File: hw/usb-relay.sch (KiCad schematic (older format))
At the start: 22 parts, among them IC1 ATTINY85-P, K1 RELAY_2RT, P1 USB_B, P2 CONN_02X03, Q1 BC548, U1 LM741

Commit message: Changes
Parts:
- removed U1: LM741, Housings_DIP:DIP-8_W7.62mm, symbol LM741
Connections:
- wire segments 67 -> 56
- no-connect marks 6 -> 4
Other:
- moved on the sheet: R2, R3
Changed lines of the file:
@@
 L R R3
 U 1 1 56BF31DE
-P 4950 6100
-F 0 "R3" V 5030 6100 50  0000 C CNN
-F 1 "R" V 4950 6100 50  0000 C CNN
-F 2 "Resistors_ThroughHole:Resistor_Horizontal_RM10mm" V 4880 6100 50  0001 C CNN
-F 3 "" H 4950 6100 50  0000 C CNN
-	1    4950 6100
+P 3850 6000
+F 0 "R3" V 3930 6000 50  0000 C CNN
+F 1 "R" V 3850 6000 50  0000 C CNN
+F 2 "Resistors_ThroughHole:Resistor_Horizontal_RM10mm" V 3780 6000 50  0001 C CNN
+F 3 "" H 3850 6000 50  0000 C CNN
+	1    3850 6000
 	0    1    1    0
 $EndComp
@@
 L R R2
 U 1 1 56BF32F5
-P 4750 6250
-F 0 "R2" V 4830 6250 50  0000 C CNN
-F 1 "R" V 4750 6250 50  0000 C CNN
-F 2 "Resistors_ThroughHole:Resistor_Horizontal_RM10mm" V 4680 6250 50  0001 C CNN
-F 3 "" H 4750 6250 50  0000 C CNN
-	1    4750 6250
+P 3550 6100
+F 0 "R2" V 3630 6100 50  0000 C CNN
+F 1 "R" V 3550 6100 50  0000 C CNN
+F 2 "Resistors_ThroughHole:Resistor_Horizontal_RM10mm" V 3480 6100 50  0001 C CNN
+F 3 "" H 3550 6100 50  0000 C CNN
+	1    3550 6100
 	1    0    0    -1
 $EndComp
@@
 $EndComp
 $Comp
-L LM741 U1
-U 1 1 56BF4D2D
-P 5050 5450
-F 0 "U1" H 5050 5700 50  0000 L CNN
-F 1 "LM741" H 5050 5600 50  0000 L CNN
-F 2 "Housings_DIP:DIP-8_W7.62mm" H 5100 5500 50  0001 C CNN
-F 3 "" H 5200 5600 50  0000 C CNN
-	1    5050 5450
-	1    0    0    -1
-$EndComp
-$Comp
 L +5V #PWR03
 U 1 1 56BF5036
@@
 Wire Wire Line
 	3050 5300 3050 3900
-Wire Wire Line
-	3050 5300 4600 5300
-Wire Wire Line
-	4600 5300 4600 5350
-Wire Wire Line
-	4600 5350 4750 5350
-$Comp
-L +5V #PWR09
-U 1 1 56BF672A
-P 4950 5100
-F 0 "#PWR09" H 4950 4950 50  0001 C CNN
-F 1 "+5V" H 4950 5240 50  0000 C CNN
-F 2 "" H 4950 5100 50  0000 C CNN
-F 3 "" H 4950 5100 50  0000 C CNN
-	1    4950 5100
-	1    0    0    -1
-$EndComp
-$Comp
-L GND #PWR010
-U 1 1 56BF69E4
-P 4950 5800
-F 0 "#PWR010" H 4950 5550 50  0001 C CNN
-F 1 "GND" H 4950 5650 50  0000 C CNN
-F 2 "" H 4950 5800 50  0000 C CNN
-F 3 "" H 4950 5800 50  0000 C CNN
-	1    4950 5800
-	1    0    0    -1
-$EndComp
 $Comp
 L C C1
@@
 Connection ~ 5100 1750
 Wire Wire Line
-	4950 5150 4950 5100
-Wire Wire Line
-	4750 5550 4750 6100
-Wire Wire Line
-	4750 6100 4800 6100
-Wire Wire Line
-	5400 6100 5100 6100
-Wire Wire Line
-	5400 4250 5400 6100
-Wire Wire Line
-	5400 5450 5350 5450
-Wire Wire Line
-	4950 5750 4950 5800
-NoConn ~ 5050 5750
-NoConn ~ 5150 5750
-Wire Wire Line
-	4750 6400 2700 6400
-Wire Wire Line
 	2700 6400 2700 5650
-Wire Wire Line
-	2700 5650 3050 5650
 Connection ~ 3050 5650
 Wire Wire Line
@@
 Wire Wire Line
 	5950 4250 5400 4250
-Connection ~ 5400 5450
 Wire Wire Line
 	5650 3900 5650 4050
@@
 	5650 4150 5750 4150
 Connection ~ 5750 4150
+Wire Wire Line
+	2700 5650 3050 5650
 $EndSCHEMATC

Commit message: Almost done, needs component values
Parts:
- removed R1, R2, R3: R, Resistors_ThroughHole:Resistor_Horizontal_RM10mm, symbol R
- added C3, C4: C, Capacitors_ThroughHole:C_Disc_D3_P2.5, symbol C
- added U1: ACS714, Housings_SOIC:SOIC-8_3.9x4.9mm_Pitch1.27mm, symbol ACS714
- renumbered R4 to R1, R5 to R2, R6 to R3, R7 to R4
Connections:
- net labels added: ADCIN, ICTL
- wire segments 56 -> 59
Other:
- moved on the sheet: D1, F1, K1, P_IN1, P_OUT1, Q1

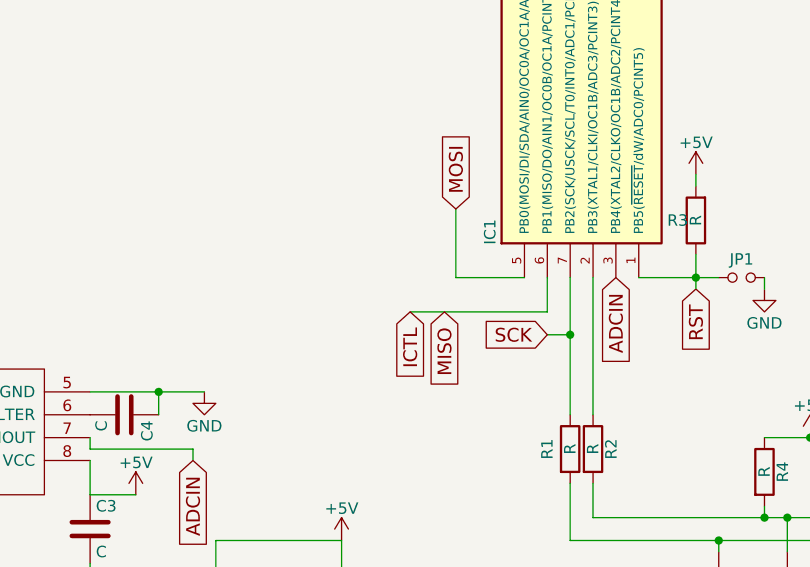
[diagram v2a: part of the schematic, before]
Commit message: Add a LED on MOSI pin, why not?
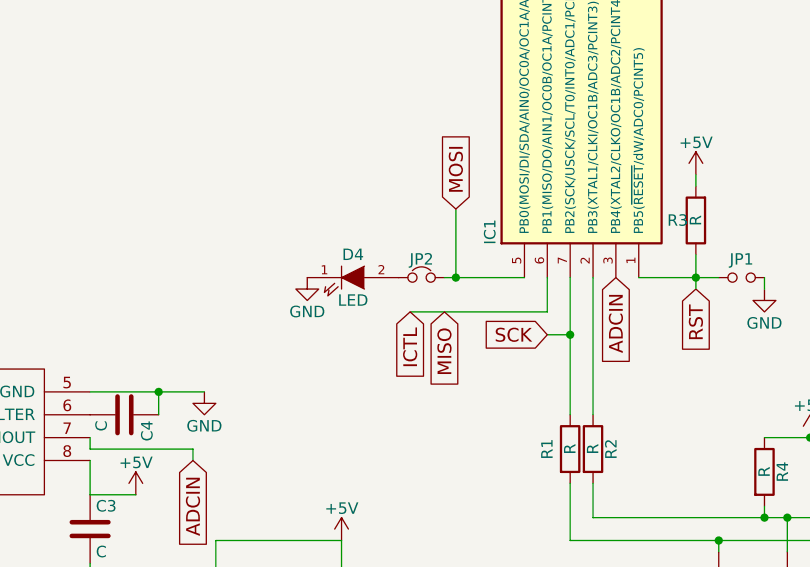
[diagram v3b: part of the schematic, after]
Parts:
- added D4: LED, LEDs:LED-5MM, symbol LED
- added JP2: Jumper_NC_Small, Pin_Headers:Pin_Header_Straight_1x02, symbol Jumper_NC_Small
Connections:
- net GND: now also D4.1 (K)
- net MOSI: now also JP2.2
- new net: D4.2 (A), JP2.1
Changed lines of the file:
@@
 RST
 Wire Wire Line
-	5550 3900 5250 3900
+	5200 3900 5550 3900
 Wire Wire Line
 	5250 3900 5250 3600
@@
 	2550 4600 2550 5800
 Connection ~ 2550 4700
+$Comp
+L LED D4
+U 1 1 56D5D510
+P 4800 3900
+F 0 "D4" H 4800 4000 50  0000 C CNN
+F 1 "LED" H 4800 3800 50  0000 C CNN
+F 2 "LEDs:LED-5MM" H 4800 3900 50  0001 C CNN
+F 3 "" H 4800 3900 50  0000 C CNN
+	1    4800 3900
+	1    0    0    -1
+$EndComp
+$Comp
+L GND #PWR015
+U 1 1 56D5D56F
+P 4600 3900
+F 0 "#PWR015" H 4600 3650 50  0001 C CNN
+F 1 "GND" H 4600 3750 50  0000 C CNN
+F 2 "" H 4600 3900 50  0000 C CNN
+F 3 "" H 4600 3900 50  0000 C CNN
+	1    4600 3900
+	1    0    0    -1
+$EndComp
+Connection ~ 5250 3900
+$Comp
+L Jumper_NC_Small JP2
+U 1 1 56D5D828
+P 5100 3900
+F 0 "JP2" H 5100 3980 50  0000 C CNN
+F 1 "Jumper_NC_Small" H 5110 3840 50  0001 C CNN
+F 2 "Pin_Headers:Pin_Header_Straight_1x02" H 5100 3900 50  0001 C CNN
+F 3 "" H 5100 3900 50  0000 C CNN
+	1    5100 3900
+	1    0    0    -1
+$EndComp
 $EndSCHEMATC

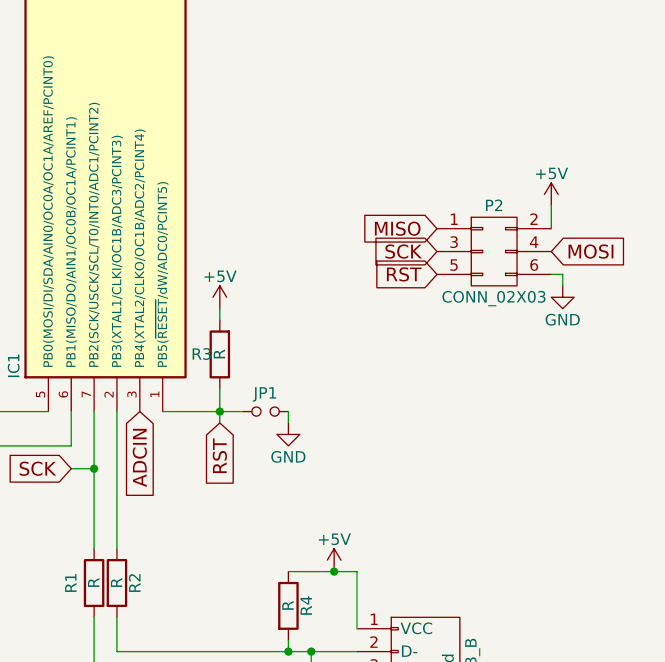
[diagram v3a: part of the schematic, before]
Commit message: Remove the reset jumper
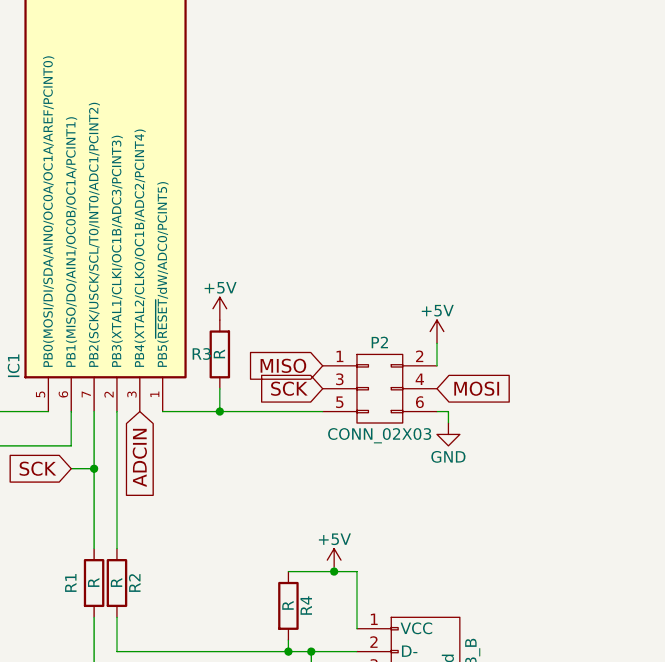
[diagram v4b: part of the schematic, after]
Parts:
- removed JP1: Jumper_NO_Small, Pin_Headers:Pin_Header_Straight_1x02, symbol Jumper_NO_Small
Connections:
- net RST: no longer names the net of IC1.1 (PB5(~RESET~/dW/ADC0/PCINT5)), P2.5 (P5), R3.1
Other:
- moved on the sheet: P2
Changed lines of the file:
@@
-$EndComp
-$Comp
-L Jumper_NO_Small JP1
-U 1 1 56BF5BE5
-P 6500 3900
-F 0 "JP1" H 6500 3980 50  0000 C CNN
-F 1 "Jumper_NO_Small" H 6510 3840 50  0001 C CNN
-F 2 "Pin_Headers:Pin_Header_Straight_1x02" H 6500 3900 50  0001 C CNN
-F 3 "" H 6500 3900 50  0000 C CNN
-	1    6500 3900
-	1    0    0    -1
 $EndComp
 $Comp
 L +5V #PWR07
 U 1 1 56BF5CD4
-P 6300 3450
-F 0 "#PWR07" H 6300 3300 50  0001 C CNN
-F 1 "+5V" H 6300 3590 50  0000 C CNN
-F 2 "" H 6300 3450 50  0000 C CNN
-F 3 "" H 6300 3450 50  0000 C CNN
-	1    6300 3450
-	1    0    0    -1
-$EndComp
-$Comp
-L GND #PWR08
-U 1 1 56BF5D12
-P 6600 3950
-F 0 "#PWR08" H 6600 3700 50  0001 C CNN
-F 1 "GND" H 6600 3800 50  0000 C CNN
-F 2 "" H 6600 3950 50  0000 C CNN
-F 3 "" H 6600 3950 50  0000 C CNN
-	1    6600 3950
+P 6300 3500
+F 0 "#PWR07" H 6300 3350 50  0001 C CNN
+F 1 "+5V" H 6300 3640 50  0000 C CNN
+F 2 "" H 6300 3500 50  0000 C CNN
+F 3 "" H 6300 3500 50  0000 C CNN
+	1    6300 3500
 	1    0    0    -1
 $EndComp
@@
 Wire Wire Line
 	6900 4600 6900 4850
-Wire Wire Line
-	6050 3900 6400 3900
-Wire Wire Line
-	6300 3800 6300 3950
-Connection ~ 6300 3900
-Wire Wire Line
-	6600 3900 6600 3950
-Wire Wire Line
-	6300 3500 6300 3450
 Connection ~ 6900 5350
 Wire Wire Line
@@
 L CONN_02X03 P2
 U 1 1 56C200ED
-P 7500 3200
-F 0 "P2" H 7500 3400 50  0000 C CNN
-F 1 "CONN_02X03" H 7500 3000 50  0000 C CNN
-F 2 "Pin_Headers:Pin_Header_Straight_2x03" H 7500 2000 50  0001 C CNN
-F 3 "" H 7500 2000 50  0000 C CNN
-	1    7500 3200
-	1    0    0    -1
-$EndComp
-Text GLabel 7250 3100 0    60   Input ~ 0
+P 7000 3800
+F 0 "P2" H 7000 4000 50  0000 C CNN
+F 1 "CONN_02X03" H 7000 3600 50  0000 C CNN
+F 2 "Pin_Headers:Pin_Header_Straight_2x03" H 7000 2600 50  0001 C CNN
+F 3 "" H 7000 2600 50  0000 C CNN
+	1    7000 3800
+	1    0    0    -1
+$EndComp
+Text GLabel 6750 3700 0    60   Input ~ 0
 MISO
-Text GLabel 7250 3200 0    60   Input ~ 0
+Text GLabel 6750 3800 0    60   Input ~ 0
 SCK
-Text GLabel 7250 3300 0    60   Input ~ 0
-RST
-Text GLabel 7750 3200 2    60   Input ~ 0
+Text GLabel 7250 3800 2    60   Input ~ 0
 MOSI
 $Comp
 L +5V #PWR010
 U 1 1 56C20428
-P 7750 3000
-F 0 "#PWR010" H 7750 2850 50  0001 C CNN
-F 1 "+5V" H 7750 3140 50  0000 C CNN
-F 2 "" H 7750 3000 50  0000 C CNN
-F 3 "" H 7750 3000 50  0000 C CNN
-	1    7750 3000
+P 7250 3600
+F 0 "#PWR010" H 7250 3450 50  0001 C CNN
+F 1 "+5V" H 7250 3740 50  0000 C CNN
+F 2 "" H 7250 3600 50  0000 C CNN
+F 3 "" H 7250 3600 50  0000 C CNN
+	1    7250 3600
 	1    0    0    -1
 $EndComp
@@
 L GND #PWR011
 U 1 1 56C20468
-P 7800 3350
-F 0 "#PWR011" H 7800 3100 50  0001 C CNN
-F 1 "GND" H 7800 3200 50  0000 C CNN
-F 2 "" H 7800 3350 50  0000 C CNN
-F 3 "" H 7800 3350 50  0000 C CNN
-	1    7800 3350
-	1    0    0    -1
-$EndComp
-Wire Wire Line
-	7750 3100 7750 3000
-Wire Wire Line
-	7750 3300 7800 3300
-Wire Wire Line
-	7800 3300 7800 3350
-Text GLabel 6300 3950 3    60   Input ~ 0
-RST
+P 7300 3950
+F 0 "#PWR011" H 7300 3700 50  0001 C CNN
+F 1 "GND" H 7300 3800 50  0000 C CNN
+F 2 "" H 7300 3950 50  0000 C CNN
+F 3 "" H 7300 3950 50  0000 C CNN
+	1    7300 3950
+	1    0    0    -1
+$EndComp
+Wire Wire Line
+	7250 3700 7250 3600
+Wire Wire Line
+	7250 3900 7300 3900
+Wire Wire Line
+	7300 3900 7300 3950
 Wire Wire Line
 	5200 3900 5550 3900
@@
 	1    0    0    -1
 $EndComp
+Wire Wire Line
+	6050 3900 6750 3900
+Wire Wire Line
+	6300 3800 6300 3900
+Connection ~ 6300 3900
 $EndSCHEMATC
